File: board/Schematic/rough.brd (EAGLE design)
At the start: 52 x 53 mm, 14 parts

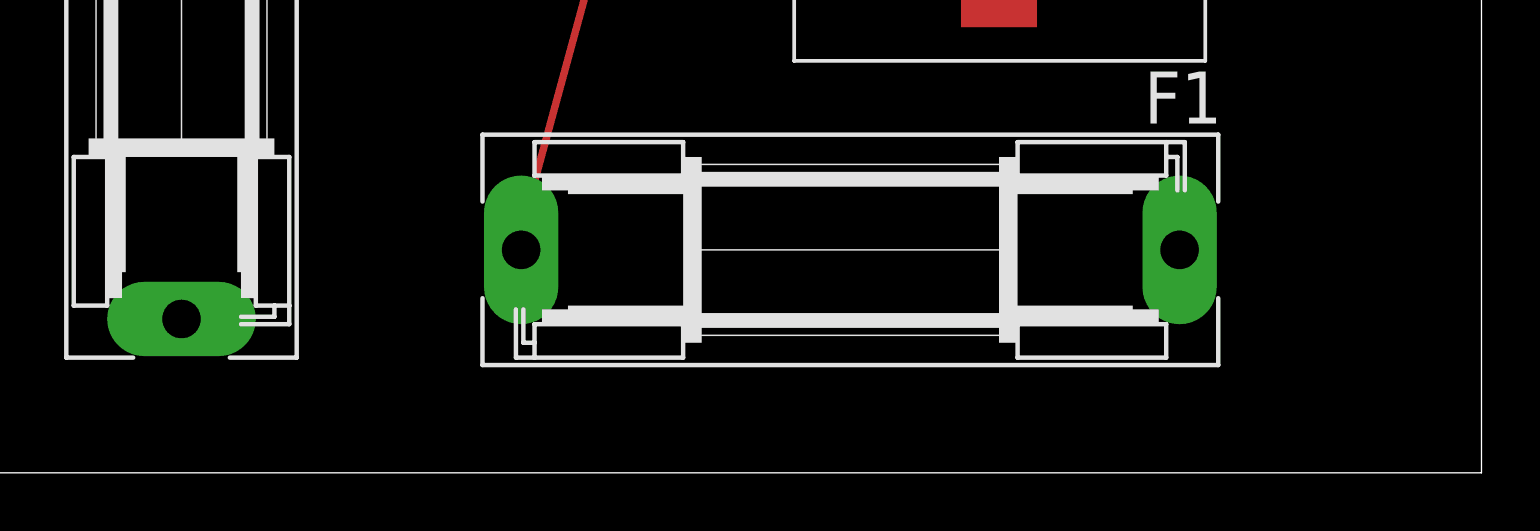
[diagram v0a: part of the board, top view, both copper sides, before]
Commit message: added surface mount pads for Vin and Vbat
yep
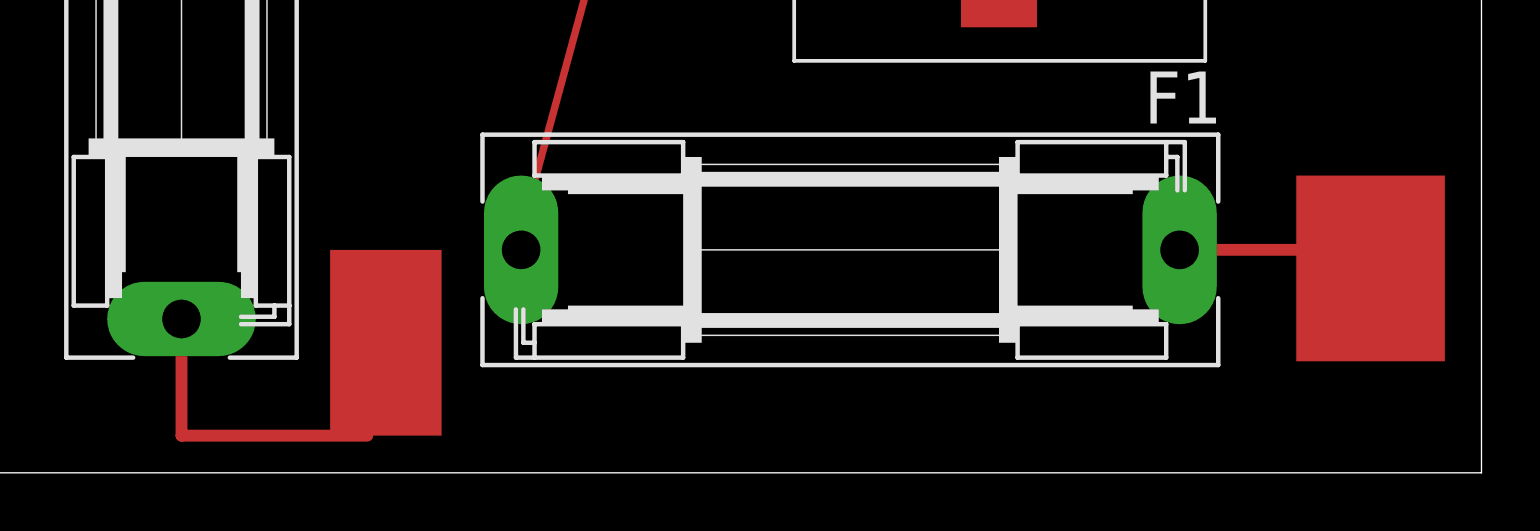
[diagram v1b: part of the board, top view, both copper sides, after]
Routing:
- net N$9: track 0.00 -> 10.2 mm
- net N$8: track 0.00 -> 3.81 mm
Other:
- board text added: "NIV"
- board text added: "TAdV"
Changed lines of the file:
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@@
 <wire x1="52.05" y1="53.01" x2="0" y2="53.01" width="0" layer="20"/>
 <wire x1="0" y1="53.01" x2="0" y2="0" width="0" layer="20"/>
+<rectangle x1="45.72" y1="3.81" x2="50.8" y2="10.16" layer="1"/>
+<rectangle x1="12.7" y1="1.27" x2="16.51" y2="7.62" layer="1"/>
+<text x="50.8" y="11.43" size="1.778" layer="22" rot="MR0">TAdV</text>
+<text x="16.51" y="8.89" size="1.778" layer="22" rot="MR0">NIV</text>
 </plain>
 <attributes>
@@
 <wire x1="7.62" y1="27.7622" x2="7.62" y2="27.94" width="0.254" layer="1"/>
 </signal>
+<signal name="N$8">
+<wire x1="41.91" y1="7.62" x2="45.72" y2="7.62" width="0.4064" layer="1"/>
+</signal>
+<signal name="N$9">
+<wire x1="7.62" y1="5.08" x2="7.62" y2="1.27" width="0.4064" layer="1"/>
+<wire x1="7.62" y1="1.27" x2="13.97" y2="1.27" width="0.4064" layer="1"/>
+</signal>
 </signals>

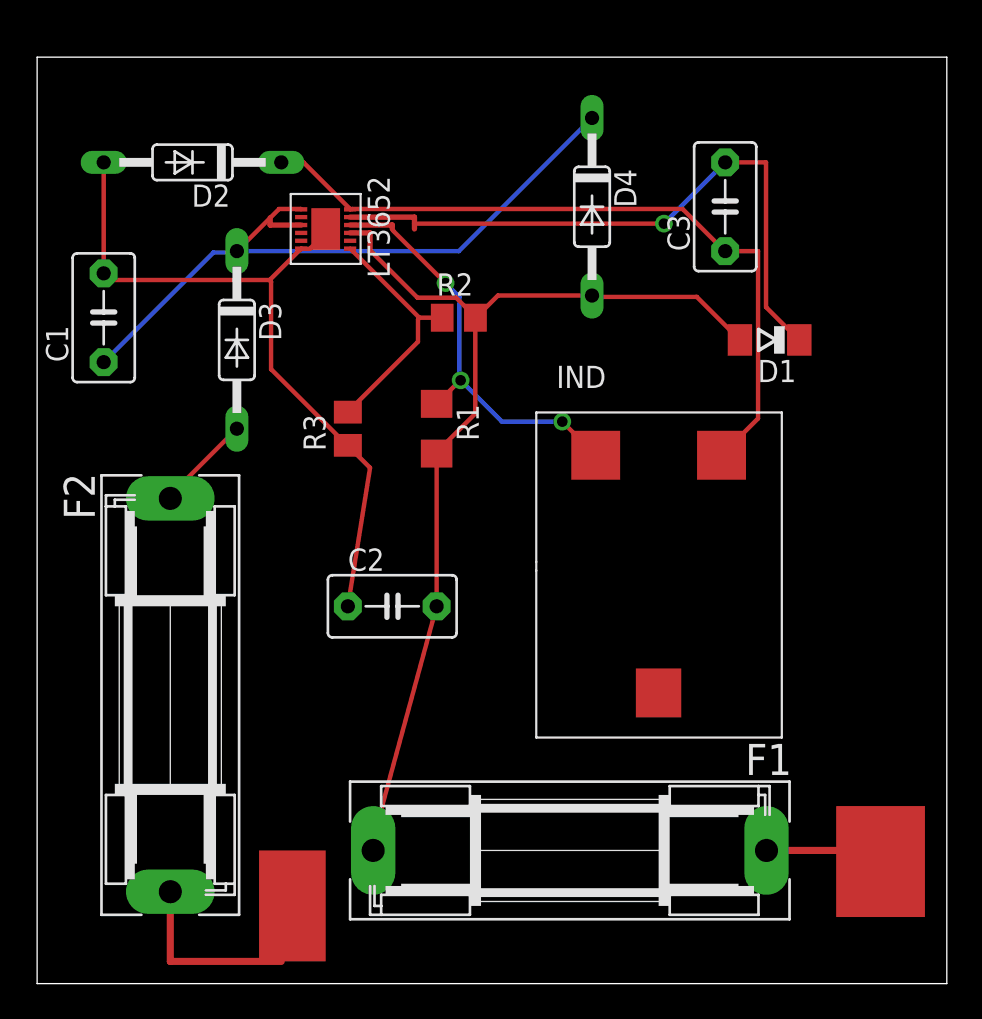
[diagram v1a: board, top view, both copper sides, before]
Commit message: finalized board. Gerber files. Board has been ordered
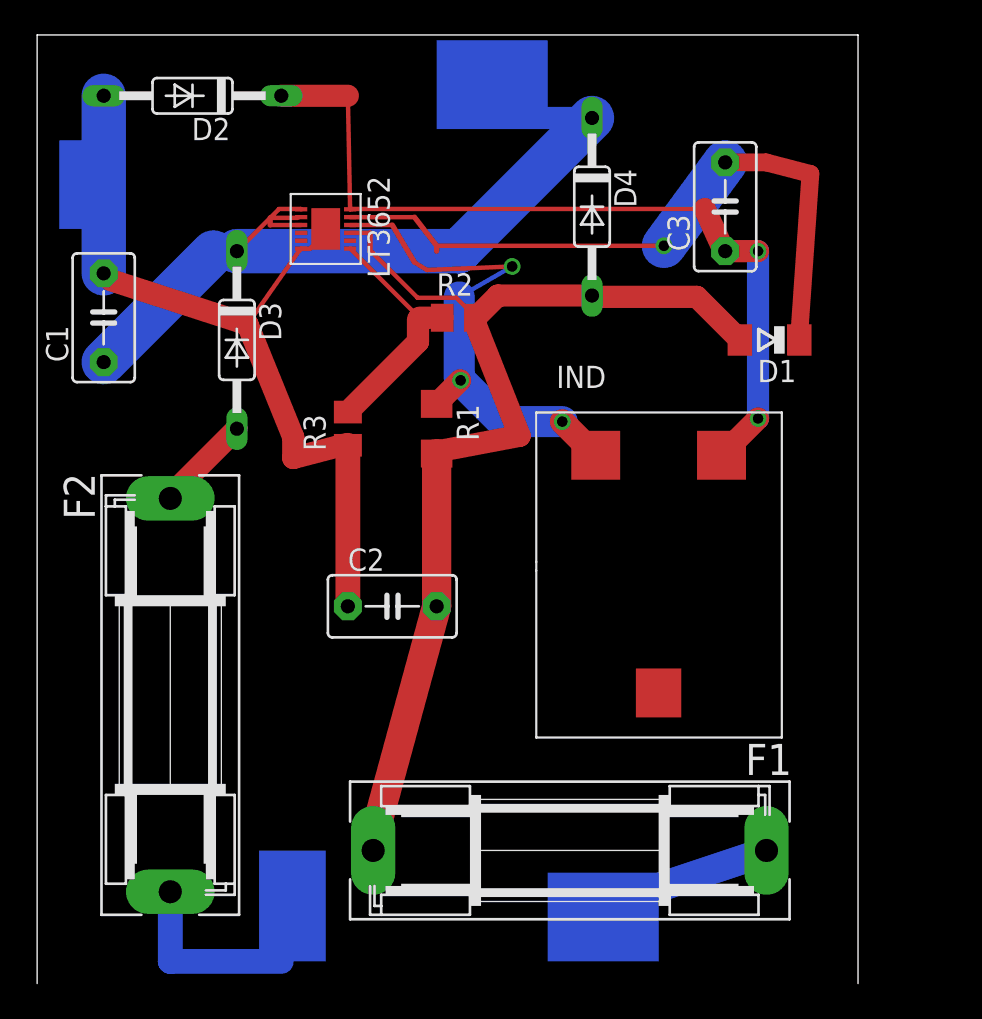
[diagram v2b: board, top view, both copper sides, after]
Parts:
- moved D2 3.81 mm to (8.89, 50.8)
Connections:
- net N$1: now also U$1.VIN_REG
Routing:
- net N$3: track 24.3 -> 30.3 mm
- net N$4: track 41.9 -> 47.7 mm, vias 0 -> 2
- net GND: track 41.7 -> 46.9 mm
- net N$8: track 3.81 -> 8.03 mm
- net N$1: track 40.6 -> 44.7 mm
- net N$2: track 59.2 -> 62.6 mm
- net N$5: track 36.9 -> 39.5 mm
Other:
- board size 52 x 53 mm -> 47 x 54.3 mm
- board text added: "Colin Gagich & Dominik Kaukinen hitchBOT Charging Circuit www.hitchbot.me - 2014"
- board text added: "GND"
- board text added: "Vbat"
- board text added: "Vin"
- board text added: "Vout"
- board text removed: "NIV"
- board text removed: "TAdV"
